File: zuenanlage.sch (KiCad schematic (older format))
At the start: 0 parts

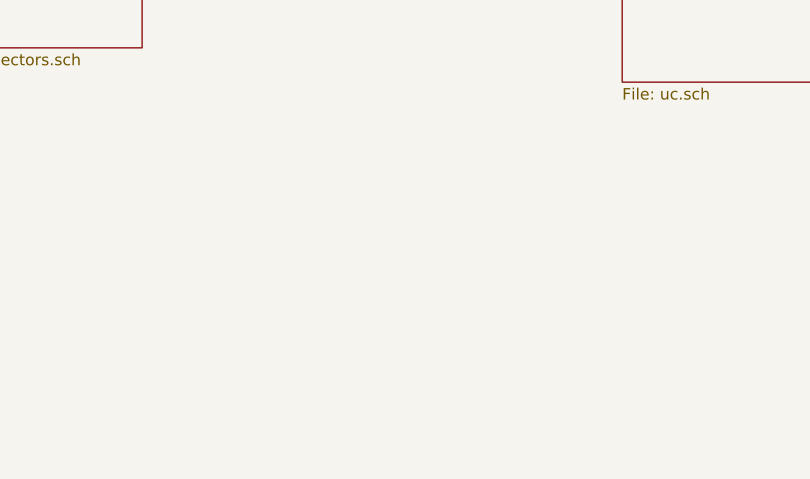
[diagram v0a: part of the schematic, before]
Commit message: added current measurement
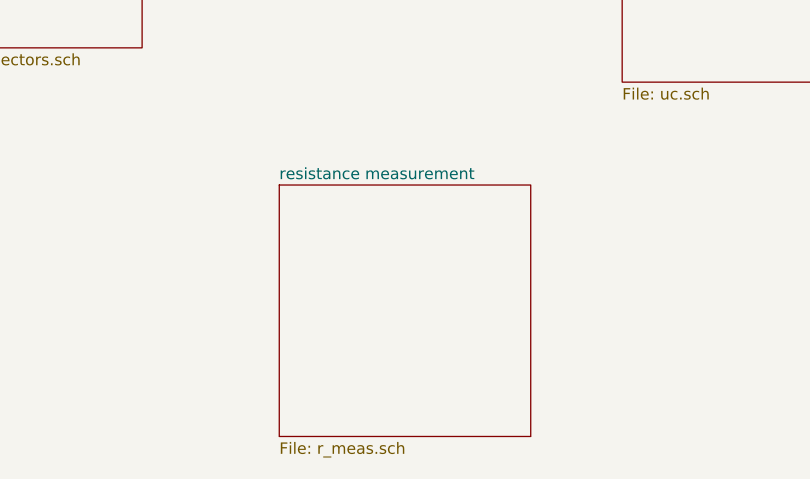
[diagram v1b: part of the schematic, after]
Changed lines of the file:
@@
 $Descr A4 11693 8268
 encoding utf-8
-Sheet 1 4
+Sheet 1 5
 Title ""
 Date ""
@@
 F1 "connectors.sch" 50
 $EndSheet
+$Sheet
+S 3350 5700 1100 1100
+U 5D5C8F4D
+F0 "resistance measurement" 50
+F1 "r_meas.sch" 50
+$EndSheet
 $EndSCHEMATC

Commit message: finished schematic for review
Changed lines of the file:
@@
 $EndDescr
 $Sheet
-S 4850 1600 1400 3650
+S 4900 1600 1400 3650
 U 5D1E53B8
 F0 "uc" 50
 F1 "uc.sch" 50
-$EndSheet
-$Sheet
-S 8600 2900 1350 1150
+F2 "CH_1" O L 4900 2050 50
+F3 "CH_2" O L 4900 2150 50
+F4 "CH_3" O L 4900 2250 50
+F5 "CH_4" O L 4900 2350 50
+F6 "CH_5" O L 4900 2450 50
+F7 "CH_6" O L 4900 2550 50
+F8 "CH_7" O L 4900 2650 50
+F9 "CH_8" O L 4900 2750 50
+F10 "CH_9" O L 4900 2850 50
+F11 "CH_10" O L 4900 2950 50
+F12 "CH_11" O L 4900 3050 50
+F13 "CH_12" O L 4900 3150 50
+F14 "CH_13" O L 4900 3250 50
+F15 "CH_14" O L 4900 3350 50
+F16 "CH_15" O L 4900 3450 50
+F17 "Ign_sup_en-1" O R 6300 3750 50
+F18 "Ign_sup_en-2" O R 6300 3850 50
+F19 "PPS_in" I L 4900 3700 50
+F20 "RS485_B" B L 4900 3950 50
+F21 "RS485_A" B L 4900 3850 50
+F22 "SDA" I L 4900 4850 50
+F23 "SCL" I L 4900 4700 50
+F24 "ADC_Ready" O L 4900 5000 50
+$EndSheet
+$Sheet
+S 8650 3550 1350 1150
 U 5D2135F9
 F0 "supply" 50
 F1 "supply.sch" 50
-$EndSheet
-$Sheet
-S 1800 2450 950  2650
+F2 "enable_DCDC-1" I L 8650 3750 50
+F3 "enable_DCDC-2" I L 8650 3850 50
+$EndSheet
+$Sheet
+S 1250 1800 950  2650
 U 5D36F340
 F0 "connectors" 50
 F1 "connectors.sch" 50
-$EndSheet
-$Sheet
-S 3350 5700 1100 1100
+F2 "Ch_5" I R 2200 2350 50
+F3 "Ch_6" I R 2200 2450 50
+F4 "Ch_7" I R 2200 2550 50
+F5 "Ch_8" I R 2200 2650 50
+F6 "Ch_1" I R 2200 1950 50
+F7 "Ch_2" I R 2200 2050 50
+F8 "Ch_3" I R 2200 2150 50
+F9 "Ch_4" I R 2200 2250 50
+F10 "Ch_9" I R 2200 2750 50
+F11 "Ch_10" I R 2200 2850 50
+F12 "Ch_11" I R 2200 2950 50
+F13 "Ch_12" I R 2200 3050 50
+F14 "PPS" O R 2200 3700 50
+F15 "Ch_13" I R 2200 3150 50
+F16 "Ch_14" I R 2200 3250 50
+F17 "Ch_15" I R 2200 3350 50
+F18 "RS485_A" I R 2200 3850 50
+F19 "RS485_B" I R 2200 3950 50
+$EndSheet
+$Sheet
+S 2700 4450 1100 1100
 U 5D5C8F4D
 F0 "resistance measurement" 50
 F1 "r_meas.sch" 50
-$EndSheet
+F2 "SCL" B R 3800 4700 50
+F3 "SDA" B R 3800 4850 50
+F4 "ADC_rdy" O R 3800 5000 50
+$EndSheet
+Wire Wire Line
+	2200 3700 4900 3700
+Wire Wire Line
+	2200 3850 4900 3850
+Wire Wire Line
+	2200 3950 4900 3950
+Wire Wire Line
+	2200 3350 2500 3350
+Text Label 2500 3350 2    50   ~ 0
+CH_15
+Wire Wire Line
+	2200 3250 2500 3250
+Text Label 2500 3250 2    50   ~ 0
+CH_14
+Wire Wire Line
+	2200 3150 2500 3150
+Text Label 2500 3150 2    50   ~ 0
+CH_13
+Wire Wire Line
+	2200 3050 2500 3050
+Text Label 2500 3050 2    50   ~ 0
+CH_12
+Wire Wire Line
+	2200 2950 2500 2950
+Text Label 2500 2950 2    50   ~ 0
+CH_11
+Wire Wire Line
+	2200 2850 2500 2850
+Text Label 2500 2850 2    50   ~ 0
+CH_10
+Wire Wire Line
+	2200 2750 2500 2750
+Text Label 2500 2750 2    50   ~ 0
+CH_9
+Wire Wire Line
+	2200 2650 2500 2650
+Text Label 2500 2650 2    50   ~ 0
+CH_8
+Wire Wire Line
+	2200 2550 2500 2550
+Text Label 2500 2550 2    50   ~ 0
+CH_7
+Wire Wire Line
+	2200 2450 2500 2450
+Text Label 2500 2450 2    50   ~ 0
+CH_6
+Wire Wire Line
+	2200 2350 2500 2350
+Text Label 2500 2350 2    50   ~ 0
+CH_5
+Wire Wire Line
+	2200 2250 2500 2250
+Text Label 2500 2250 2    50   ~ 0
+CH_4
+Wire Wire Line
+	2200 2150 2500 2150
+Text Label 2500 2150 2    50   ~ 0
+CH_3
+Wire Wire Line
+	2200 2050 2500 2050
+Text Label 2500 2050 2    50   ~ 0
+CH_2
+Wire Wire Line
+	2200 1950 2500 1950
+Text Label 2500 1950 2    50   ~ 0
+CH_1
+Wire Wire Line
+	4900 3450 4600 3450
+Text Label 4600 3450 0    50   ~ 0
+CH_15
+Wire Wire Line
+	4900 3350 4600 3350
+Text Label 4600 3350 0    50   ~ 0
+CH_14
+Wire Wire Line
+	4900 3250 4600 3250
+Text Label 4600 3250 0    50   ~ 0
+CH_13
+Wire Wire Line
+	4900 3150 4600 3150
+Text Label 4600 3150 0    50   ~ 0
+CH_12
+Wire Wire Line
+	4900 3050 4600 3050
+Text Label 4600 3050 0    50   ~ 0
+CH_11
+Wire Wire Line
+	4900 2950 4600 2950
+Text Label 4600 2950 0    50   ~ 0
+CH_10
+Wire Wire Line
+	4900 2850 4600 2850
+Text Label 4600 2850 0    50   ~ 0
+CH_9
+Wire Wire Line
+	4900 2750 4600 2750
+Text Label 4600 2750 0    50   ~ 0
+CH_8
+Wire Wire Line
+	4900 2650 4600 2650
+Text Label 4600 2650 0    50   ~ 0
+CH_7
+Wire Wire Line
+	4900 2550 4600 2550
+Text Label 4600 2550 0    50   ~ 0
+CH_6
+Wire Wire Line
+	4900 2450 4600 2450
+Text Label 4600 2450 0    50   ~ 0
+CH_5
+Wire Wire Line
+	4900 2350 4600 2350
+Text Label 4600 2350 0    50   ~ 0
+CH_4
+Wire Wire Line
+	4900 2250 4600 2250
+Text Label 4600 2250 0    50   ~ 0
+CH_3
+Wire Wire Line
+	4900 2150 4600 2150
+Text Label 4600 2150 0    50   ~ 0
+CH_2
+Wire Wire Line
+	4900 2050 4600 2050
+Text Label 4600 2050 0    50   ~ 0
+CH_1
+Wire Wire Line
+	6300 3750 8650 3750
+Wire Wire Line
+	6300 3850 8650 3850
+Wire Wire Line
+	3800 4700 4900 4700
+Wire Wire Line
+	3800 4850 4900 4850
+Wire Wire Line
+	3800 5000 4900 5000
 $EndSCHEMATC
